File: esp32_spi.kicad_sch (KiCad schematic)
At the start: 29 parts, among them J1 Conn_01x06_Female, J2 Conn_02x06_Odd_Even, SW1 SW_Push, SW2 SW_Push, U201 SN74LV1T34, U202 SN74LV1T34, U203 74AHCT595, U204 SN74LV1T34, U205 74AHCT595, U206 ESP32-WROOM-32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

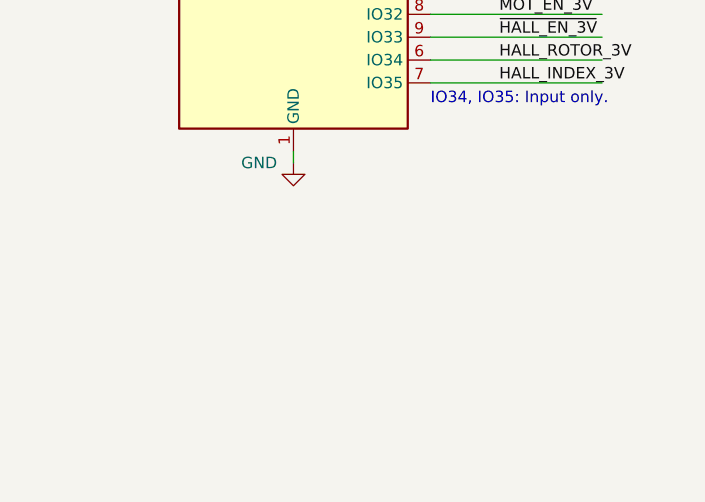
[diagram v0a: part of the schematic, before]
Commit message: add Display sheet and I2C Pullups
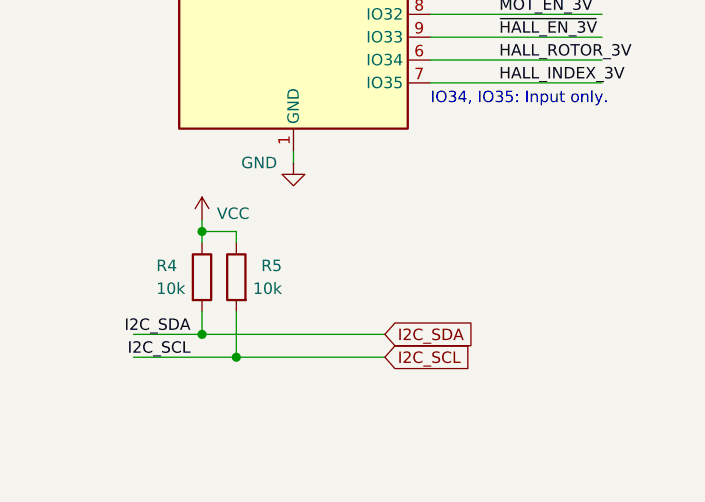
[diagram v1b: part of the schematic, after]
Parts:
- added R4, R5: 10k, Resistor_SMD:R_0603_1608Metric, symbol Device:R
- C200: Link https://www.reichelt.de/smd-vielschicht-keramikkondensator-100n-10--x7r-g0603-100n-p31873.html?&trstct=pos_1&nbc=1 -> https://www.reichelt.de/smd-vielschicht-keramikkondensator-100n-10--x7r-g0603-100n-p31873.html?&trstct=pos_3&nbc=1
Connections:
- net I2C_SCL: now also R5.2
- net I2C_SDA: now also R4.2
- net VCC: now also R4.1, R5.1
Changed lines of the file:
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@@
   (paper "A4")
   (junction (at 34.29 48.26) (diameter 1.016) (color 0 0 0 0))
+  (junction (at 38.1 163.83) (diameter 1.016) (color 0 0 0 0))
+  (junction (at 38.1 175.26) (diameter 1.016) (color 0 0 0 0))
   (junction (at 39.37 19.05) (diameter 1.016) (color 0 0 0 0))
   (junction (at 39.37 35.56) (diameter 1.016) (color 0 0 0 0))
+  (junction (at 41.91 177.8) (diameter 1.016) (color 0 0 0 0))
   (junction (at 43.18 38.1) (diameter 1.016) (color 0 0 0 0))
   (junction (at 86.36 24.13) (diameter 1.016) (color 0 0 0 0))
@@
   (junction (at 204.47 147.32) (diameter 1.016) (color 0 0 0 0))
   (junction (at 220.98 24.13) (diameter 1.016) (color 0 0 0 0))
-  (no_connect (at 33.02 127))
   (no_connect (at 33.02 129.54))
   (no_connect (at 33.02 96.52))
+  (no_connect (at 33.02 127))
   (no_connect (at 33.02 132.08))
+  (no_connect (at 33.02 121.92))
+  (no_connect (at 63.5 93.98))
   (no_connect (at 33.02 124.46))
-  (no_connect (at 33.02 121.92))
+  (no_connect (at 33.02 93.98))
   (no_connect (at 33.02 119.38))
-  (no_connect (at 33.02 93.98))
-  (no_connect (at 63.5 93.98))
   (wire (pts (xy 19.05 88.9) (xy 33.02 88.9))
     (stroke (width 0) (type solid) (color 0 0 0 0))
@@
     (stroke (width 0) (type solid) (color 0 0 0 0))
   )
+  (wire (pts (xy 30.48 175.26) (xy 38.1 175.26))
+    (stroke (width 0) (type solid) (color 0 0 0 0))
+  )
+  (wire (pts (xy 30.48 177.8) (xy 41.91 177.8))
+    (stroke (width 0) (type solid) (color 0 0 0 0))
+  )
   (wire (pts (xy 34.29 44.45) (xy 35.56 44.45))
     (stroke (width 0) (type solid) (color 0 0 0 0))
@@
     (stroke (width 0) (type solid) (color 0 0 0 0))
   )
+  (wire (pts (xy 38.1 162.56) (xy 38.1 163.83))
+    (stroke (width 0) (type solid) (color 0 0 0 0))
+  )
+  (wire (pts (xy 38.1 163.83) (xy 38.1 165.1))
+    (stroke (width 0) (type solid) (color 0 0 0 0))
+  )
+  (wire (pts (xy 38.1 163.83) (xy 41.91 163.83))
+    (stroke (width 0) (type solid) (color 0 0 0 0))
+  )
+  (wire (pts (xy 38.1 172.72) (xy 38.1 175.26))
+    (stroke (width 0) (type solid) (color 0 0 0 0))
+  )
+  (wire (pts (xy 38.1 175.26) (xy 58.42 175.26))
+    (stroke (width 0) (type solid) (color 0 0 0 0))
+  )
   (wire (pts (xy 39.37 17.78) (xy 39.37 19.05))
     (stroke (width 0) (type solid) (color 0 0 0 0))
@@
   )
   (wire (pts (xy 39.37 35.56) (xy 54.61 35.56))
+    (stroke (width 0) (type solid) (color 0 0 0 0))
+  )
+  (wire (pts (xy 41.91 163.83) (xy 41.91 165.1))
+    (stroke (width 0) (type solid) (color 0 0 0 0))
+  )
+  (wire (pts (xy 41.91 172.72) (xy 41.91 177.8))
+    (stroke (width 0) (type solid) (color 0 0 0 0))
+  )
+  (wire (pts (xy 41.91 177.8) (xy 58.42 177.8))
     (stroke (width 0) (type solid) (color 0 0 0 0))
   )
@@
     (effects (font (size 1.27 1.27)) (justify left bottom))
   )
+  (label "I2C_SDA" (at 36.83 175.26 180)
+    (effects (font (size 1.27 1.27)) (justify right bottom))
+  )
+  (label "I2C_SCL" (at 36.83 177.8 180)
+    (effects (font (size 1.27 1.27)) (justify right bottom))
+  )
   (label "ESP32_RX" (at 45.72 30.48 0)
     (effects (font (size 1.27 1.27)) (justify left bottom))
@@
   (label "SPI_CLK" (at 208.28 137.16 0)
     (effects (font (size 1.27 1.27)) (justify left bottom))
+  )
+  (global_label "I2C_SDA" (shape input) (at 58.42 175.26 0)    (property "Intersheet References" "${INTERSHEET_REFS}" (id 0) (at 69.9771 175.1806 0)
+      (effects (font (size 1.27 1.27)) (justify left) hide)
+    )
+    (effects (font (size 1.27 1.27)) (justify left))
+  )
+  (global_label "I2C_SCL" (shape input) (at 58.42 177.8 0)    (property "Intersheet References" "${INTERSHEET_REFS}" (id 0) (at 69.9166 177.7206 0)
+      (effects (font (size 1.27 1.27)) (justify left) hide)
+    )
+    (effects (font (size 1.27 1.27)) (justify left))
   )
   (global_label "ABCDEF_HALL_ROTOR" (shape input) (at 156.21 62.23 180)    (property "Intersheet References" "${INTERSHEET_REFS}" (id 0) (at 132.5577 62.1506 0)
@@
     )
   )
+  (symbol (lib_id "power:VCC") (at 38.1 162.56 0) (unit 1)
+    (in_bom yes) (on_board yes)
+    (property "Reference" "#PWR0115" (id 0) (at 38.1 166.37 0)
+      (effects (font (size 1.27 1.27)) hide)
+    )
+    (property "Value" "VCC" (id 1) (at 39.751 161.8488 0)
+      (effects (font (size 1.27 1.27)) (justify left))
+    )
+    (property "Footprint" "" (id 2) (at 38.1 162.56 0)
+      (effects (font (size 1.27 1.27)) hide)
+    )
+    (property "Datasheet" "" (id 3) (at 38.1 162.56 0)
+      (effects (font (size 1.27 1.27)) hide)
+    )
+  )
   (symbol (lib_id "power:VCC") (at 39.37 17.78 0) (unit 1)
     (in_bom yes) (on_board yes)
@@
     )
   )
+  (symbol (lib_id "Device:R") (at 38.1 168.91 0) (unit 1)
+    (in_bom yes) (on_board yes)
+    (property "Reference" "R4" (id 0) (at 33.02 167.64 0)
+      (effects (font (size 1.27 1.27)) (justify left))
+    )
+    (property "Value" "10k" (id 1) (at 33.02 170.18 0)
+      (effects (font (size 1.27 1.27)) (justify left))
+    )
+    (property "Footprint" "Resistor_SMD:R_0603_1608Metric" (id 2) (at 36.322 168.91 90)
+      (effects (font (size 1.27 1.27)) hide)
+    )
+    (property "Datasheet" "~" (id 3) (at 38.1 168.91 0)
+      (effects (font (size 1.27 1.27)) hide)
+    )
+  )
   (symbol (lib_id "Device:R") (at 39.37 24.13 0) (unit 1)
     (in_bom yes) (on_board yes)
@@
     )
   )
+  (symbol (lib_id "Device:R") (at 41.91 168.91 0) (mirror y) (unit 1)
+    (in_bom yes) (on_board yes)
+    (property "Reference" "R5" (id 0) (at 46.99 167.64 0)
+      (effects (font (size 1.27 1.27)) (justify left))
+    )
+    (property "Value" "10k" (id 1) (at 46.99 170.18 0)
+      (effects (font (size 1.27 1.27)) (justify left))
+    )
+    (property "Footprint" "Resistor_SMD:R_0603_1608Metric" (id 2) (at 43.688 168.91 90)
+      (effects (font (size 1.27 1.27)) hide)
+    )
+    (property "Datasheet" "~" (id 3) (at 41.91 168.91 0)
+      (effects (font (size 1.27 1.27)) hide)
+    )
+  )
   (symbol (lib_id "Device:R") (at 43.18 24.13 0) (mirror y) (unit 1)
     (in_bom yes) (on_board yes)
@@
       (effects (font (size 1.27 1.27)) hide)
     )
-    (property "Link" "https://www.reichelt.de/smd-vielschicht-keramikkondensator-100n-10--x7r-g0603-100n-p31873.html?&trstct=pos_1&nbc=1" (id 5) (at 25.4 107.95 0)
-      (effects (font (size 1.27 1.27)) hide)
-    )
+    (property "Link" "https://www.reichelt.de/smd-vielschicht-keramikkondensator-100n-10--x7r-g0603-100n-p31873.html?&trstct=pos_3&nbc=1" (id 5) (at 25.4 107.95 0)
+      (effects (font (size 1.27 1.27)) hide)
+    )

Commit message: Display Routing
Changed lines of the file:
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@@
   (junction (at 204.47 147.32) (diameter 1.016) (color 0 0 0 0))
   (junction (at 220.98 24.13) (diameter 1.016) (color 0 0 0 0))
+  (no_connect (at 33.02 124.46))
+  (no_connect (at 33.02 96.52))
+  (no_connect (at 33.02 132.08))
   (no_connect (at 33.02 129.54))
-  (no_connect (at 33.02 96.52))
+  (no_connect (at 63.5 93.98))
   (no_connect (at 33.02 127))
-  (no_connect (at 33.02 132.08))
+  (no_connect (at 33.02 119.38))
   (no_connect (at 33.02 121.92))
-  (no_connect (at 63.5 93.98))
-  (no_connect (at 33.02 124.46))
   (no_connect (at 33.02 93.98))
-  (no_connect (at 33.02 119.38))
   (wire (pts (xy 19.05 88.9) (xy 33.02 88.9))
     (stroke (width 0) (type solid) (color 0 0 0 0))
@@
     (effects (font (size 1.27 1.27)) (justify left bottom))
   )
-  (label "I2C_SDA" (at 36.83 175.26 180)
-    (effects (font (size 1.27 1.27)) (justify right bottom))
-  )
-  (label "I2C_SCL" (at 36.83 177.8 180)
-    (effects (font (size 1.27 1.27)) (justify right bottom))
-  )
   (label "ESP32_RX" (at 45.72 30.48 0)

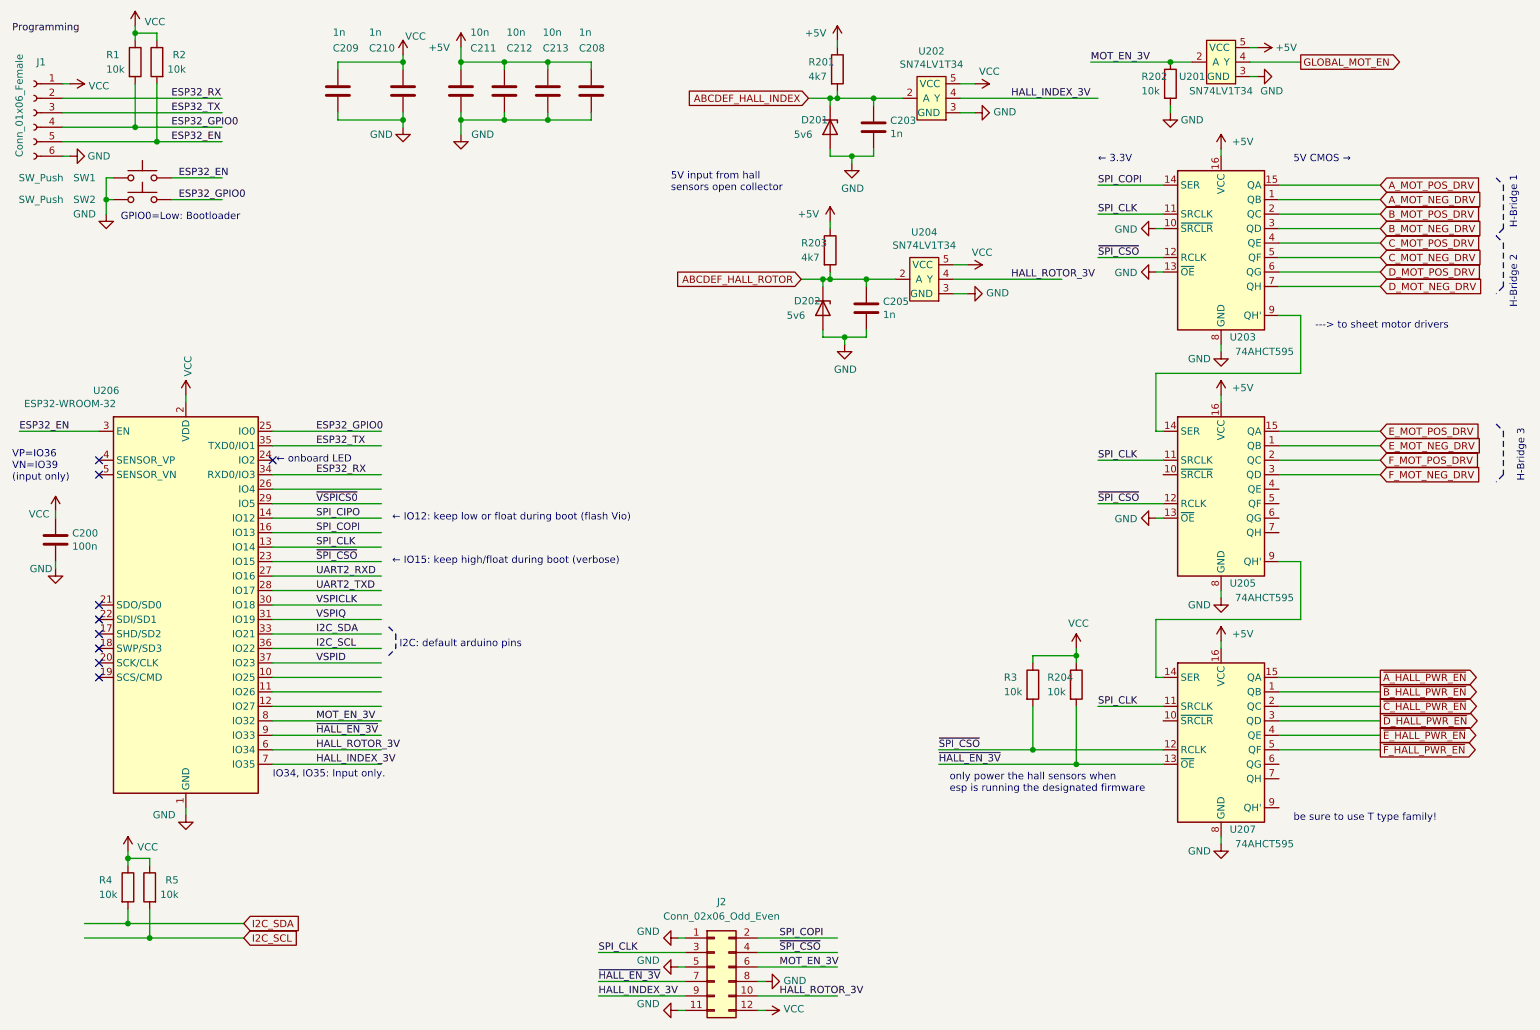
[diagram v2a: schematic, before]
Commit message: GND Vias and Bus Resistors in series.
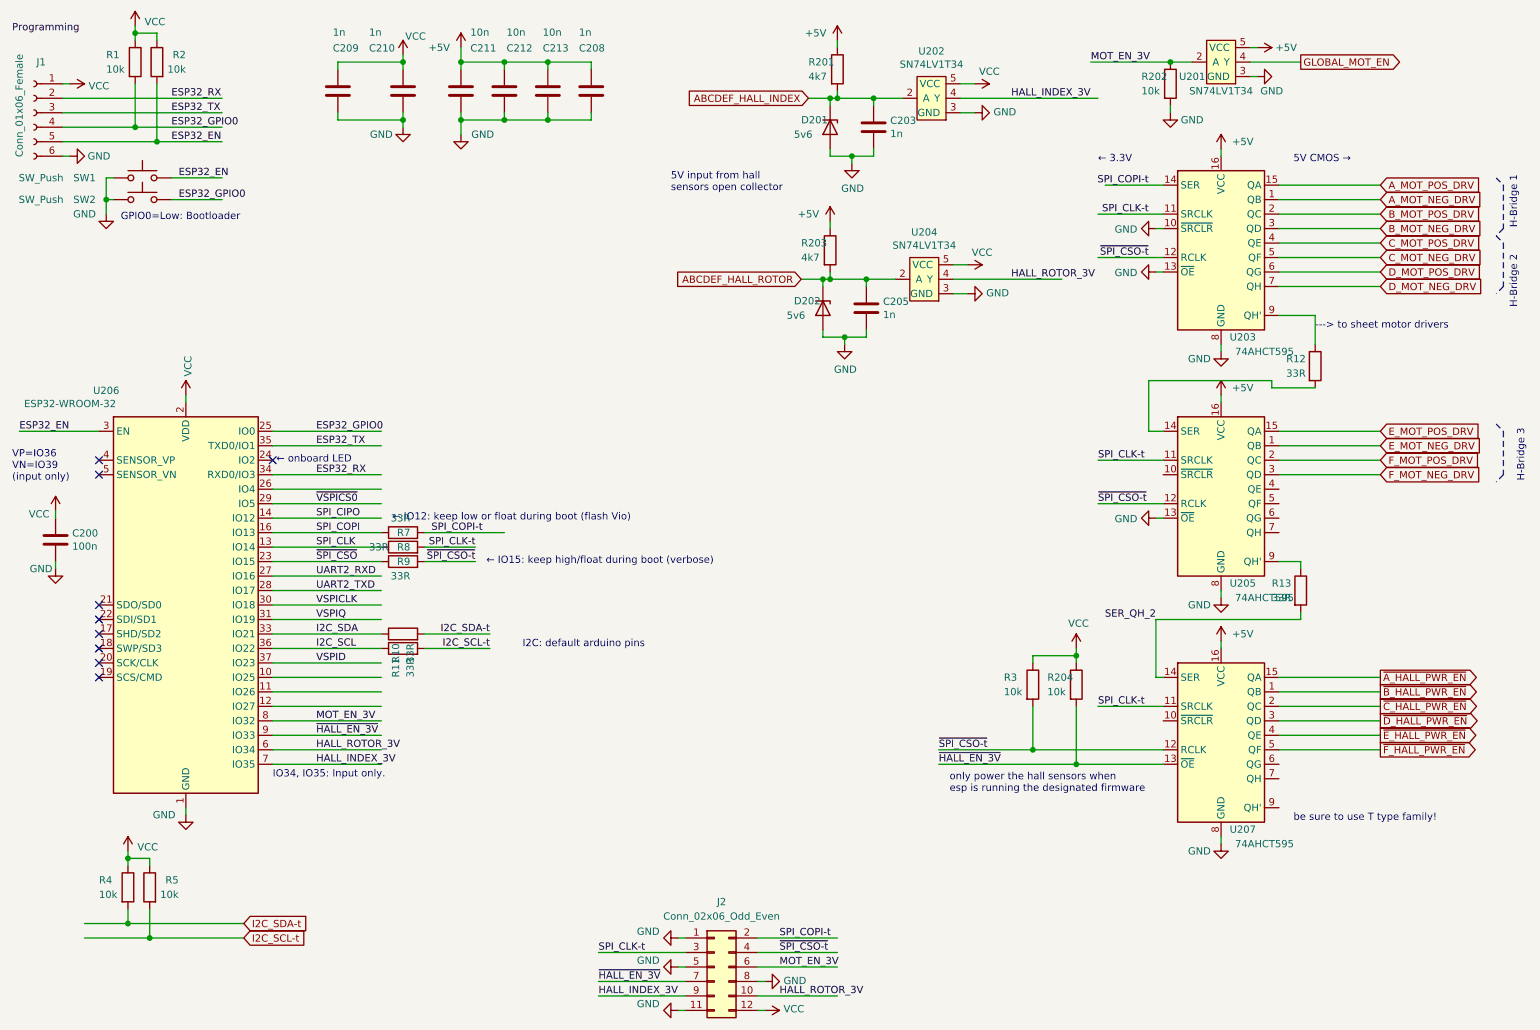
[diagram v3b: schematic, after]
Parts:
- added R10, R11, R12, R13, R7, R8, R9: 33R, Resistor_SMD:R_0603_1608Metric, symbol Device:R
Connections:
- net I2C_SCL: now also R11.1; no longer R5.2
- net I2C_SDA: now also R10.1; no longer R4.2
- net SPI_CLK: now also R8.1; no longer J2.3 (Pin_3), U203.11 (SRCLK), U205.11 (SRCLK), U207.11 (SRCLK)
- net SPI_COPI: now also R7.1; no longer J2.2 (Pin_2), U203.14 (SER)
- net ~SPI_CSO~: now also R9.1; no longer J2.4 (Pin_4), R3.2, U203.12 (RCLK), U205.12 (RCLK), U207.12 (RCLK)
- net at U203.9 (QH'): now also R12.1; no longer U205.14 (SER)
- net at U205.9 (QH'): now also R13.1; no longer U207.14 (SER)
- new net: R12.2, U205.14 (SER)
- new net I2C_SCL-t: R11.2, R5.2
- new net I2C_SDA-t: R10.2, R4.2
- new net SER_QH_2: R13.2, U207.14 (SER)
- new net SPI_CLK-t: J2.3 (Pin_3), R8.2, U203.11 (SRCLK), U205.11 (SRCLK), U207.11 (SRCLK)
- new net SPI_COPI-t: J2.2 (Pin_2), R7.2, U203.14 (SER)
- new net ~SPI_CSO-t~: J2.4 (Pin_4), R3.2, R9.2, U203.12 (RCLK), U205.12 (RCLK), U207.12 (RCLK)

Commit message: BOM
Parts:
- J2: Distri (none) -> Reichelt; Link (none) -> https://www.reichelt.de/stiftleisten-2-00-mm-2x10-gerade-mp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
- R1, R2, R202, R204, R3, R4, R5: Distri (none) -> Reichelt; Link (none) -> https://www.reichelt.de/smd-widerstand-0603-10-kohm-100-mw-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
- R10, R11, R12, R13, R7, R8, R9: Distri (none) -> Reichelt; Link (none) -> https://www.reichelt.de/smd-widerstand-0603-33-ohm-100-mw-1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
- R201, R203: Distri (none) -> Reichelt; Link (none) -> https://www.reichelt.de/smd-widerstand-0603-6-98-kohm-100-m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
- SW1, SW2: Distri (none) -> Reichelt; Link (none) -> https://www.reichelt.de/smd-kurzhubtaster-vert-montage-hoeh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
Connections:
- net GND: no longer U203.10 (~SRCLR)
